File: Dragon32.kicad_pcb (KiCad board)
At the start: 2 copper layers, 120.2 x 69.7 mm, 59 parts, among them IC1 74HCT273, IC10 74HCT32, IC11 74LS123N, IC12 LM1889N, IC13 2318, IC15 CD4053, IC2 MC6847, IC3 74HCT00, IC4 74HCT20, IC5 74HCT86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

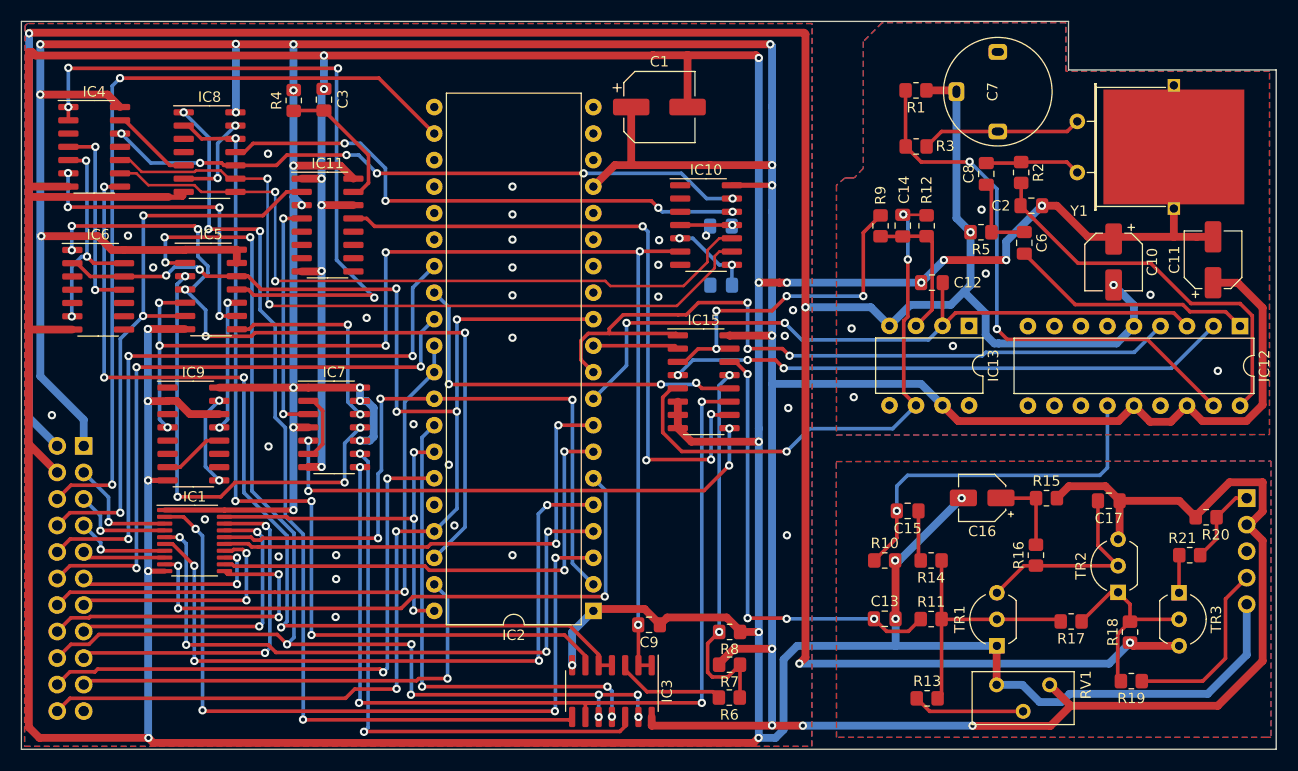
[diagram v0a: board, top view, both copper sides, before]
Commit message: add test points
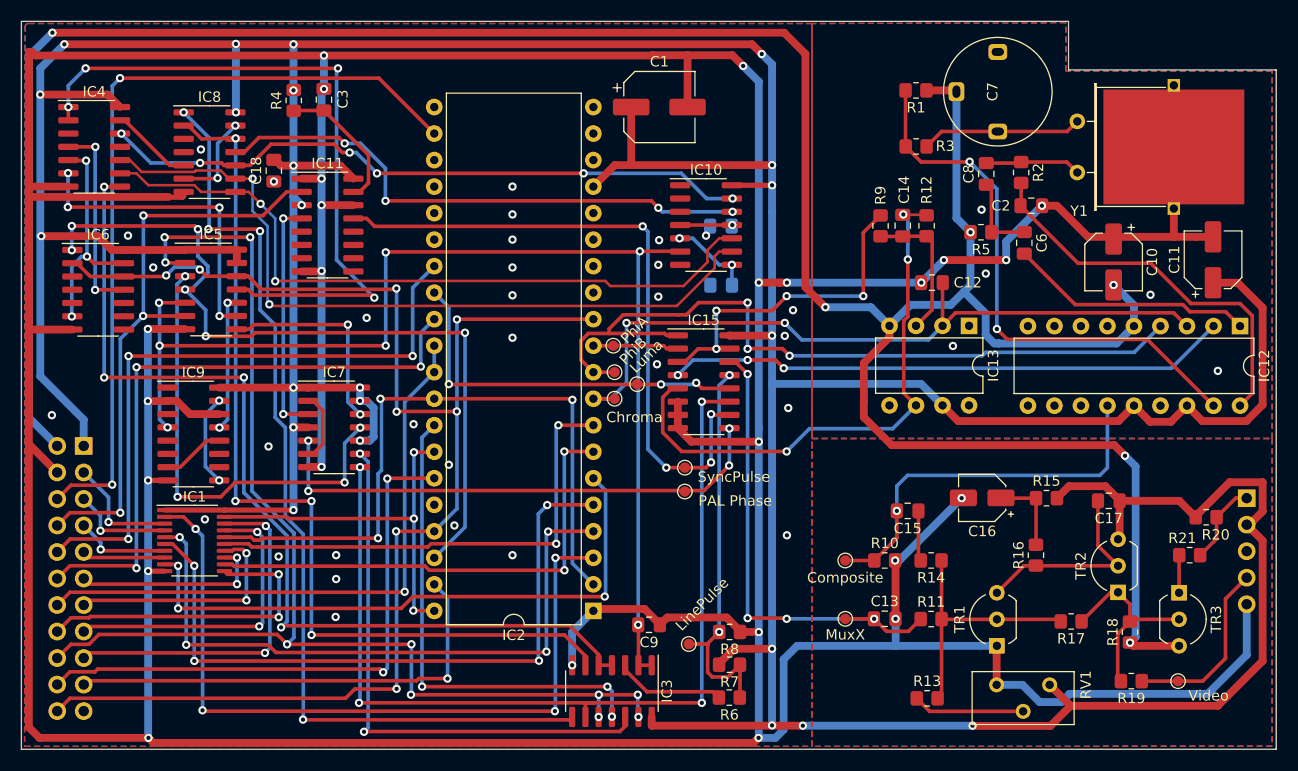
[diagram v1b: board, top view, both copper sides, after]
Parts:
- added C18: 470nF, Capacitor_SMD:C_0805_2012Metric_Pad1.18x1.45mm_HandSolder, F.Cu at (256.4, 73.8)
- added TP1: TestPoint_Luma, TestPoint:TestPoint_Pad_D1.0mm, F.Cu at (291.2, 94.2)
- added TP10: TestPoint_LinePulse, TestPoint:TestPoint_Pad_D1.0mm, F.Cu at (296.2, 119.1)
- added TP2: TestPoint_PhiA, TestPoint:TestPoint_Pad_D1.0mm, F.Cu at (288.9, 90.6)
- added TP3: TestPoint_PhiB, TestPoint:TestPoint_Pad_D1.0mm, F.Cu at (289.1, 93.1)
- added TP4: TestPoint_Chroma, TestPoint:TestPoint_Pad_D1.0mm, F.Cu at (289.1, 95.6)
- added TP5: TestPoint_Composite, TestPoint:TestPoint_Pad_D1.0mm, F.Cu at (311.1, 111.1)
- added TP6: TestPoint_MuxX, TestPoint:TestPoint_Pad_D1.0mm, F.Cu at (311.1, 116.7)
- added TP7: TestPoint_Video, TestPoint:TestPoint_Pad_D1.0mm, F.Cu at (343.0, 122.7)
- added TP8: TestPoint_SyncPulse, TestPoint:TestPoint_Pad_D1.0mm, F.Cu at (295.8, 102.2)
- added TP9: TestPoint_PALPhase, TestPoint:TestPoint_Pad_D1.0mm, F.Cu at (295.8, 104.5)
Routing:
- net -5V: track 278.0 -> 262.4 mm
- net CHB: track 68.7 -> 71.7 mm
- net Composite: track 34.9 -> 37.7 mm
- net MUX X: track 43.2 -> 46.0 mm
- net phiB: track 73.4 -> 75.4 mm
- net LINE PULSE: track 36.3 -> 38.1 mm
- net Net-(IC8B-Q3): track 70.7 -> 69.2 mm
- net GND: track 572.9 -> 571.6 mm
- net Net-(IC4-Pad1): track 68.0 -> 67.0 mm
- net Net-(IC8B-Q1): track 61.9 -> 62.8 mm
- net Net-(IC8B-Q2): track 74.3 -> 73.4 mm
- removed copper zone on B.Cu, net (none)
- removed copper zone on F.Cu, net (none)

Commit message: revise layout
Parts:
- removed IC13: 2318, Package_DIP:DIP-8_W7.62mm
- added C19: 100uF, Capacitor_SMD:CP_Elec_6.3x5.8, F.Cu at (284.8, 123.1)
- added C20: 0.01uF, Capacitor_SMD:C_0805_2012Metric_Pad1.18x1.45mm_HandSolder, B.Cu at (259.7, 93.7)
- added U1: 74AHC1G04, Package_TO_SOT_SMD:SOT-353_SC-70-5_Handsoldering, F.Cu at (291.3, 122.1)
- added U2: MCP6281, Package_TO_SOT_SMD:SOT-23-5_HandSoldering, F.Cu at (319.3, 91.5)
- C18: moved to B.Cu
- TR1, TR2: value 2N2369 -> MMBT4401; footprint Package_TO_SOT_THT:TO-92_Inline_Wide -> vdg:SOT-23-3
- TR3: value BC212 -> MMBT3906; footprint Package_TO_SOT_THT:TO-92_Inline_Wide -> vdg:SOT-23-3
- moved IC10 37.0 mm to (262.1, 88.8)
- moved C4 35.0 mm to (265.6, 88.9), turned to 0 degrees
- moved C5 34.5 mm to (265.6, 92.7), turned to 0 degrees
- moved IC3 28.8 mm to (262.1, 112.6), turned to 0 degrees
- moved TR1 3.86 mm to (325.7, 115.4)
- moved TR2 3.74 mm to (337.3, 110.4)
- moved TR3 3.66 mm to (343.2, 117.9)
- moved IC8 2.44 mm to (247.9, 71.5)
- moved IC11 2.19 mm to (261.5, 76.8)
- moved IC7 2.14 mm to (262.1, 100.5)
- moved C18 1.30 mm to (256.3, 72.5)
- moved C9 0.39 mm to (292.4, 117.7)
- moved Y1 0.29 mm to (333.4, 74.3)
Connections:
- net /~{VCLK}/16 renamed /~{VCLK}/8
- net Net-(IC8A-Q2) renamed /~{VCLK}/4
- net Net-(IC8B-Q1) renamed /~{VCLK}/32
- net Net-(IC8B-Q2) renamed /~{VCLK}/64
- net Net-(IC8B-Q3) renamed /~{VCLK}/128
- IC3 pad 1: /LINE PULSES -> unconnected-(IC3-Pad1)
- IC3 pad 2: /LINE PULSES -> unconnected-(IC3-Pad2)
- IC3 pad 3: Net-(IC3-Pad3) -> unconnected-(IC3-Pad3)
- R6 pad 2: Net-(IC3-Pad3) -> Net-(R6-Pad2)
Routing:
- net GND: track 571.6 -> 525.7 mm, vias 61 -> 56
- net Net-(IC7B-Q): track 53.3 -> 10.4 mm
- net Net-(IC3-Pad4): track 93.0 -> 59.3 mm
- net /~{VCLK}/64: track 73.4 -> 40.1 mm, vias 2 -> 4
- net /~{VCLK}/128: track 69.2 -> 36.4 mm, vias 2 -> 4
- net VCLK: track 119.7 -> 91.1 mm, vias 10 -> 7
- net Net-(IC8A-MR): track 88.4 -> 61.1 mm, vias 4 -> 2
- net CLK: track 46.3 -> 20.2 mm, vias 3 -> 1
- net +5V: track 510.6 -> 536.7 mm, vias 23 -> 27
- net /~{VCLK}: track 91.7 -> 66.1 mm
- net /~{VCLK}/32: track 62.8 -> 41.6 mm, vias 6 -> 4
- net Net-(IC8B-Q0): track 53.0 -> 34.8 mm, vias 4 -> 2
- net Net-(IC3-Pad3): track 10.5 -> 0.00 mm
- net Net-(R6-Pad2): track 0.00 -> 9.95 mm
- net Net-(IC4-Pad1): track 67.0 -> 59.5 mm
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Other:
- board text added: "<- DIGITAL"
- board text added: "AMP"
- board text added: "ANALOGUE ->"
- board text added: "DRAGON REV.3 PAL"
- board text added: "MODULATOR"
- board text added: "NTSC -> PAL"

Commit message: prep for fabrication
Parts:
- moved C19 148.4 mm to (136.4, 125.6)
- moved C7 148.4 mm to (177.4, 68.7)
- moved IC15 148.4 mm to (149.2, 96.5)
- moved R21 148.4 mm to (195.8, 113.1)
- moved R9 148.4 mm to (166.2, 81.5)
- moved TP3 148.4 mm to (140.7, 95.6)
- moved TP4 148.4 mm to (140.7, 98.1)
- moved TR2 148.4 mm to (188.9, 112.9)
- moved U1 148.4 mm to (143.0, 124.6)
- moved C1 148.4 mm to (145.0, 70.2)
- moved C10 148.4 mm to (188.5, 85.0)
- moved C12 148.4 mm to (171.1, 87.0)
- moved C14 148.4 mm to (168.3, 81.5)
- moved C17 148.4 mm to (188.0, 107.9)
- moved C18 148.4 mm to (107.9, 75.0)
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
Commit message: fix transistor footprints
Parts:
- moved TR1 1.54 mm to (178.8, 118.2), turned to 180 degrees
- moved TR3 0.65 mm to (194.2, 120.2), turned to 180 degrees
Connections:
- TR1 pad 1: GND -> Net-(TR1-B)
- TR1 pad 2: Net-(TR1-B) -> GND
- TR2 pad 1: Net-(TR2-E) -> Net-(TR1-C)
- TR2 pad 2: Net-(TR1-C) -> Net-(TR2-E)
- TR3 pad 1: Net-(TR3-E) -> Net-(TR2-E)
- TR3 pad 2: Net-(TR2-E) -> Net-(TR3-E)
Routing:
- net GND: track 525.7 -> 511.7 mm, vias 56 -> 54
- net Net-(TR2-E): track 21.5 -> 24.4 mm
- net Net-(TR1-B): track 27.0 -> 25.0 mm
- net -5V: track 263.9 -> 262.7 mm
- net Net-(TR1-C): track 20.4 -> 19.7 mm, vias 2 -> 0

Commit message: reformat board
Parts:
- added TP11: TestPoint_FrameSync, TestPoint:TestPoint_Pad_D1.0mm, F.Cu at (93.5, 128.7)
- added TP12: TestPoint_LineSync, TestPoint:TestPoint_Pad_D1.0mm, F.Cu at (89.8, 94.2)
- added TP13: TestPoint_VCLK, TestPoint:TestPoint_Pad_D1.0mm, F.Cu at (96.8, 128.7)
- C10, C11: footprint Capacitor_SMD:CP_Elec_5x5.8 -> Capacitor_Tantalum_SMD:CP_EIA-3528-21_Kemet-B_Pad1.50x2.35mm_HandSolder
- C3, R4: moved to B.Cu
- C7: footprint Dragon:Trimmer-7.5mm -> Dragon:Trimmer_small
- TP5: value TestPoint_Composite -> TestPoint_Chroma
- moved TP10 43.6 mm to (154.4, 78.5)
- moved R6 41.5 mm to (152.3, 85.2)
- moved C9 40.4 mm to (144.6, 79.7)
- moved R7 40.4 mm to (152.3, 83.1)
- moved U1 40.4 mm to (143.6, 84.2)
- moved R8 39.5 mm to (152.3, 81.0), turned to 0 degrees
- moved C19 13.6 mm to (148.0, 118.4), turned to 180 degrees
- moved C15 10.5 mm to (178.8, 112.0)
- moved R14 9.27 mm to (179.8, 116.5), turned to 90 degrees
- moved TP5 9.18 mm to (171.8, 112.0)
- moved R3 8.77 mm to (176.9, 78.7), turned to -90 degrees
- moved R10 7.95 mm to (174.5, 113.0), turned to -90 degrees
- moved R9 7.56 mm to (169.3, 88.4)
- moved C14 7.56 mm to (171.4, 88.4)
- moved R12 7.56 mm to (173.7, 88.4)
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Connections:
- net Composite renamed Chroma
- net Net-(C15-Pad1) renamed /Chroma_a
- net Net-(IC15-Z0) renamed /MUX Zinput
- net Net-(TR1-B) renamed /Composite_a
- net Net-(TR2-E) renamed /Composite_b
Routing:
- net GND: track 511.7 -> 39.9 mm, vias 54 -> 38
- net /LINE PULSES: track 109.7 -> 74.8 mm, vias 7 -> 5
- net LINE PULSE: track 38.1 -> 21.3 mm
- net -5V: track 262.7 -> 278.2 mm, vias 8 -> 6
- net VCLK: track 91.1 -> 98.2 mm, vias 7 -> 9
- net /Composite_a: track 25.0 -> 18.1 mm
- net +5V: track 536.6 -> 543.2 mm, vias 27 -> 20
- net Chroma: track 37.7 -> 31.7 mm, vias 1 -> 0
- net Net-(TR1-C): track 19.7 -> 13.9 mm
- net CHB: track 73.4 -> 78.5 mm
- net phiB: track 76.0 -> 71.2 mm
- net Net-(IC4-Pad1): track 59.5 -> 55.1 mm
- net ChrOSC: track 53.0 -> 48.7 mm
- net DA0: track 77.4 -> 73.3 mm
- net MUX X: track 46.0 -> 41.9 mm, vias 4 -> 2
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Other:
- board size 120.2 x 69.7 mm -> 120 x 65.8 mm

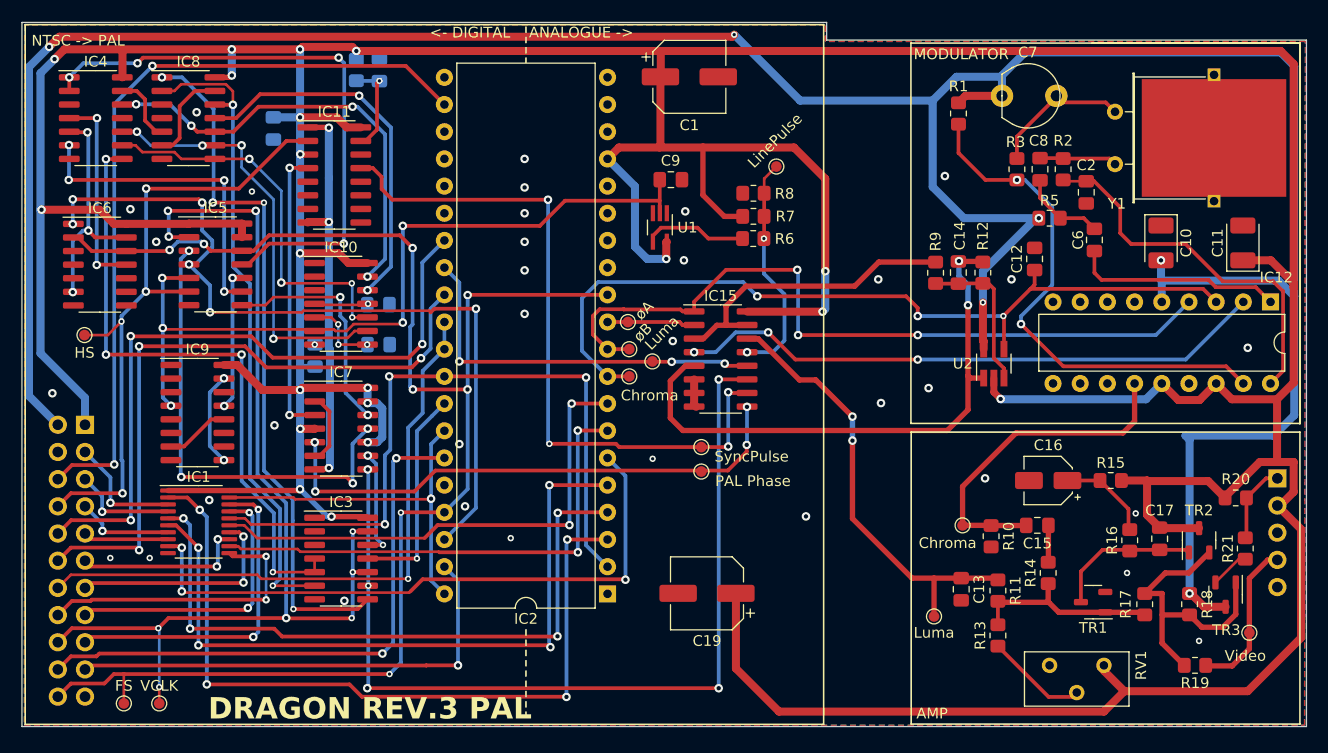
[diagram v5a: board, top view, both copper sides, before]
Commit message: supplement power filtering
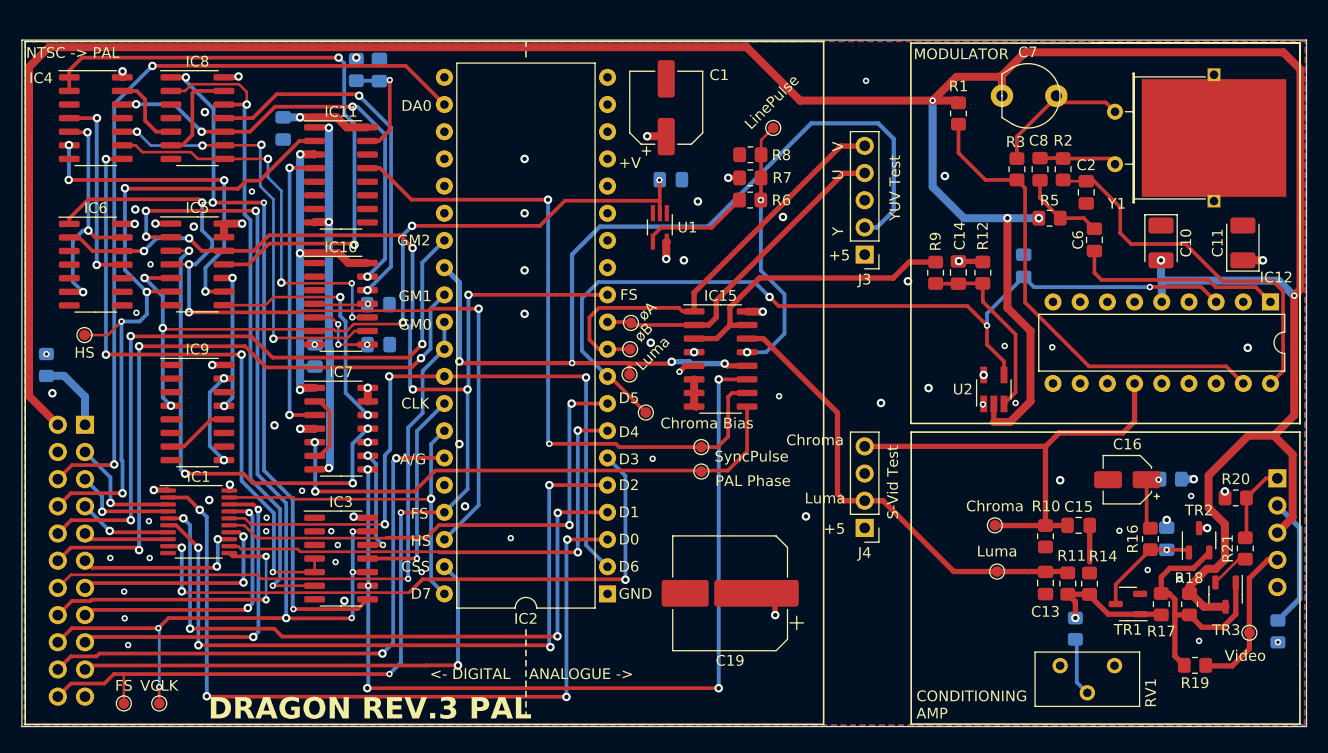
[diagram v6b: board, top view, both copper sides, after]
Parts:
- added FB1: FerriteBead_Small, Inductor_SMD:L_0805_2012Metric_Pad1.15x1.40mm_HandSolder, B.Cu at (86.2, 97.0)
- added FB2: FerriteBead_Small, Inductor_SMD:L_0805_2012Metric_Pad1.15x1.40mm_HandSolder, B.Cu at (201.3, 121.9)
- added J3: YUV Output, Connector_PinHeader_2.54mm:PinHeader_1x05_P2.54mm_Vertical, F.Cu at (162.7, 86.7)
- added J4: S-Video Test, Connector_PinHeader_2.54mm:PinHeader_1x04_P2.54mm_Vertical, F.Cu at (162.7, 112.3)
- C1: value 100uF -> 10uF
- C12, C17, C9, R13, R15: moved to B.Cu
- C19: footprint Capacitor_SMD:CP_Elec_6.3x5.8 -> Dragon:CP_Elec_10x10.5
- moved C13 7.90 mm to (179.6, 117.4)
- moved C16 7.40 mm to (187.2, 107.7)
- moved R13 7.27 mm to (182.4, 121.7)
- moved TP6 7.23 mm to (175.1, 116.3)
- moved R11 6.56 mm to (181.7, 117.4)
- moved R15 5.61 mm to (191.3, 107.7)
- moved R10 5.08 mm to (179.6, 113.0)
- moved R14 3.99 mm to (183.7, 117.5)
- moved C15 3.86 mm to (182.7, 112.0)
- moved TP4 3.72 mm to (142.2, 101.5)
- moved R6 3.61 mm to (152.0, 81.6)
- moved R7 3.61 mm to (152.0, 79.5)
- moved TP10 3.61 mm to (154.1, 74.9)
- moved R8 3.61 mm to (152.0, 77.4)
- moved C1 3.61 mm to (144.1, 73.0), turned to 90 degrees
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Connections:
- J1 pad 1: +5V -> Net-(J1-Pin_1)
- J2 pad 2: +5V -> Net-(J2-Pin_2)
- J2 pad 3: unconnected-(J2-Pin_3-Pad3) -> -5V
- U2 pad 2: +5V -> -5V
- U2 pad 5: -5V -> +5V
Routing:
- net +5V: track 543.2 -> 67.8 mm, vias 20 -> 30
- net LUM: track 36.4 -> 93.5 mm, vias 3 -> 4
- net phiB: track 71.2 -> 96.1 mm, vias 3 -> 0
- net phiA: track 8.21 -> 30.9 mm
- net -5V: track 278.2 -> 293.7 mm, vias 6 -> 5
- net Net-(J2-Pin_2): track 0.00 -> 12.4 mm
- net Chroma: track 31.7 -> 43.9 mm
- net Net-(J1-Pin_1): track 0.00 -> 7.03 mm
- net /Composite_a: track 18.1 -> 11.4 mm, vias 0 -> 1
- net CHB: track 78.5 -> 83.6 mm
- net ChrOSC: track 48.7 -> 44.5 mm, vias 2 -> 0
- net Net-(R13-Pad1): track 9.50 -> 5.46 mm
- net Net-(C16-Pad1): track 8.78 -> 4.83 mm, vias 0 -> 1
- net Net-(TR1-C): track 13.9 -> 10.1 mm, vias 0 -> 1
- net Net-(IC4-Pad1): track 55.1 -> 58.7 mm, vias 4 -> 2
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- added copper zone on In2.Cu, net +5V
- added copper zone on In1.Cu, net GND
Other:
- board size 120 x 65.8 mm -> 120 x 64.1 mm
- copper layers 2 -> 4
- board text added: "+5"
- board text added: "+V"
- board text added: "A/G"
- board text added: "CLK"
- board text added: "CONDITIONING AMP"
- board text added: "CSS"
- board text added: "Chroma"
- board text added: "D0"
- board text added: "D1"
- board text added: "D2"
- board text added: "D3"
- board text added: "D4"
- board text added: "D5"
- board text added: "D6"
- board text added: "D7"
- board text added: "DA0"
- board text added: "FS"
- board text added: "GM0"
- board text added: "GM1"
- board text added: "GM2"
- board text added: "GND"
- board text added: "HS"
- board text added: "Luma"
- board text added: "S-Vid Test"
- board text added: "U"
- board text added: "V"
- board text added: "Y"
- board text added: "YUV Test"
- board text removed: "AMP"

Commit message: refinement
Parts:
- added TP14: TestPoint_SyncPulse, TestPoint:TestPoint_Pad_D1.0mm, F.Cu at (171.1, 100.7)
- U2: value MCP6281 -> TS971
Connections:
- C14 pad 1: Net-(U2-Vin+) -> Net-(U2-Vin-)
- R12 pad 1: Net-(U2-Vin+) -> Net-(U2-Vin-)
- R9 pad 2: Net-(U2-Vin+) -> Net-(U2-Vin-)
- U2 pad 3: Net-(U2-Vin+) -> CHB
- U2 pad 4: CHB -> Net-(U2-Vin-)
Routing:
- net Net-(U2-Vin+): track 17.4 -> 0.00 mm
- net Net-(U2-Vin-): track 0.00 -> 13.8 mm
- net CHB: track 83.6 -> 91.8 mm
- net /MUX Zinput: track 52.4 -> 54.6 mm
- net /Chroma_a: track 3.45 -> 4.46 mm
- net GND: vias 56 -> 55
